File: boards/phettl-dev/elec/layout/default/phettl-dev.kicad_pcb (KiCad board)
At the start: 2 copper layers, 28.9 x 29.9 mm, 16 parts, among them U1 ?, U2 ?, U3 ?, U4 ?, U5 ?, U6 ?, U7 ?

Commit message: [VENDOR] components
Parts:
- added U8: ?, lib:HM-NFC-Class6-Antenna, B.Cu at (152.6, 116.8)
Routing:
- net p010_nfc2: track 0.00 -> 5.58 mm
- net p009_nfc1: track 0.00 -> 4.88 mm, vias 0 -> 1
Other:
- board size 28.9 x 29.9 mm -> 28.9 x 49.8 mm

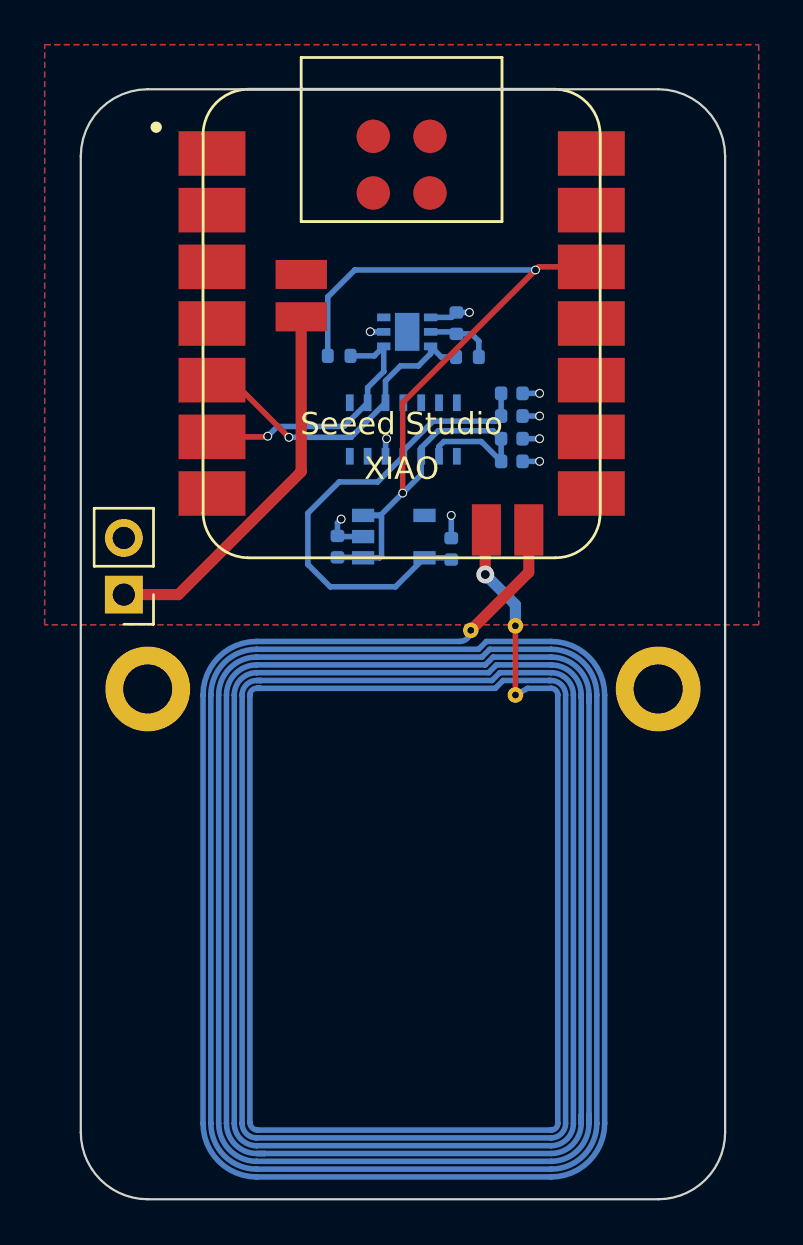
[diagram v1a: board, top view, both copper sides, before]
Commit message: [PCB] restore layout
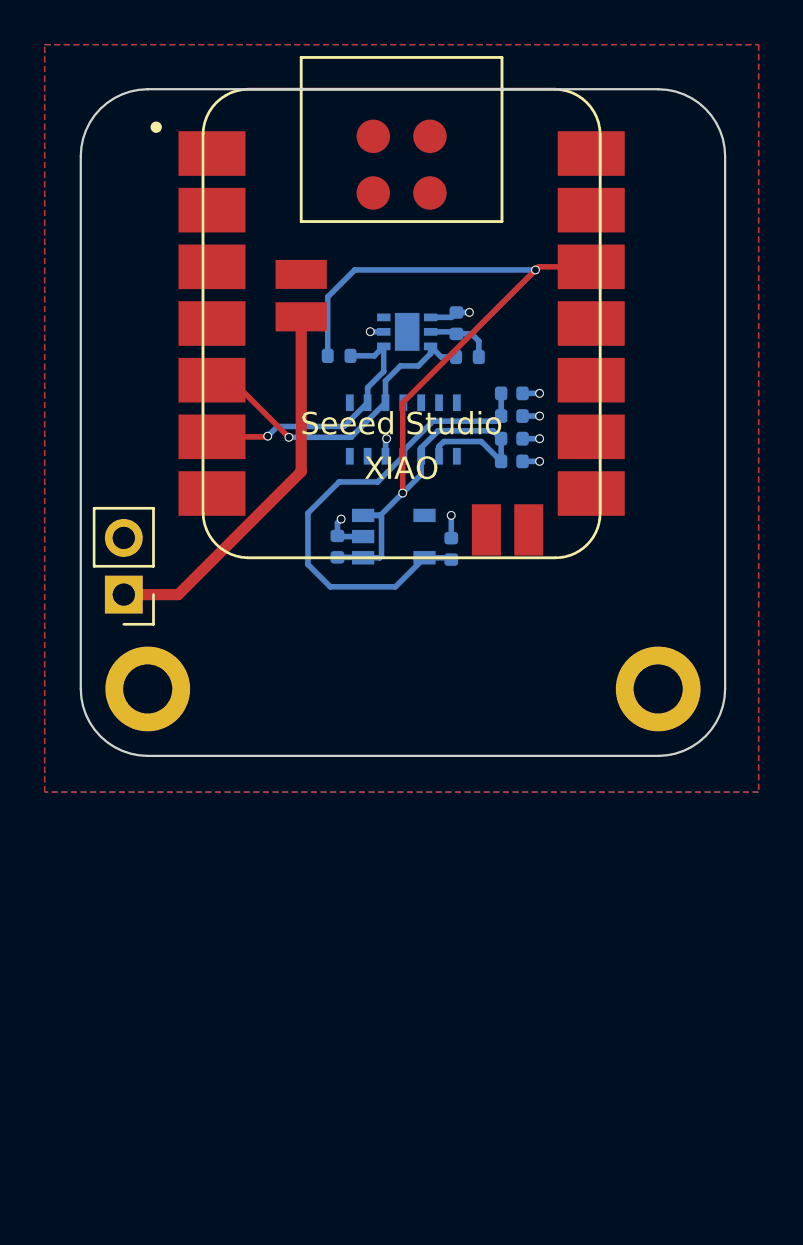
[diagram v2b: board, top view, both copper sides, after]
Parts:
- removed U8: ?, lib:HM-NFC-Class6-Antenna
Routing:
- net p010_nfc2: track 5.58 -> 0.00 mm
- net p009_nfc1: track 4.88 -> 0.00 mm, vias 1 -> 0
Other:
- board size 28.9 x 49.8 mm -> 28.9 x 29.9 mm
